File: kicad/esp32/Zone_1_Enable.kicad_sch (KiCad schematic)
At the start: 5 parts, among them SW201 B3F-1150

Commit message: Created rev 1.01 - Addes some more labels and annotations
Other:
- title: (none) -> TL2C-ESP32-1 TL2C Adapter for ESP32
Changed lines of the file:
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@@
 	(generator "eeschema")
 	(generator_version "8.0")
-	(paper "A4")
+	(paper "A3")
+	(title_block
+		(title "TL2C-ESP32-1 TL2C Adapter for ESP32")
+		(date "2024-02-08")
+		(rev "1.01")
+	)
 	(junction
 		(at 107.95 62.23)

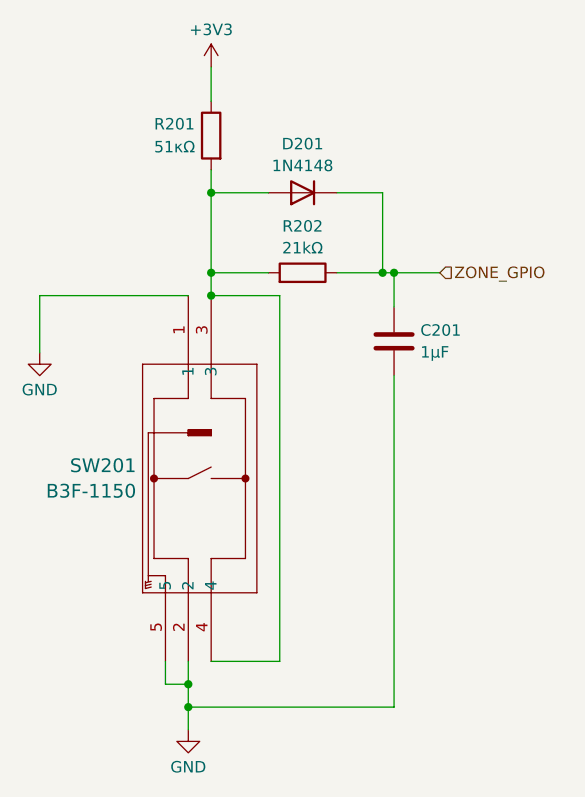
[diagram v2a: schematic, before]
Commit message: Reseated the RJ45
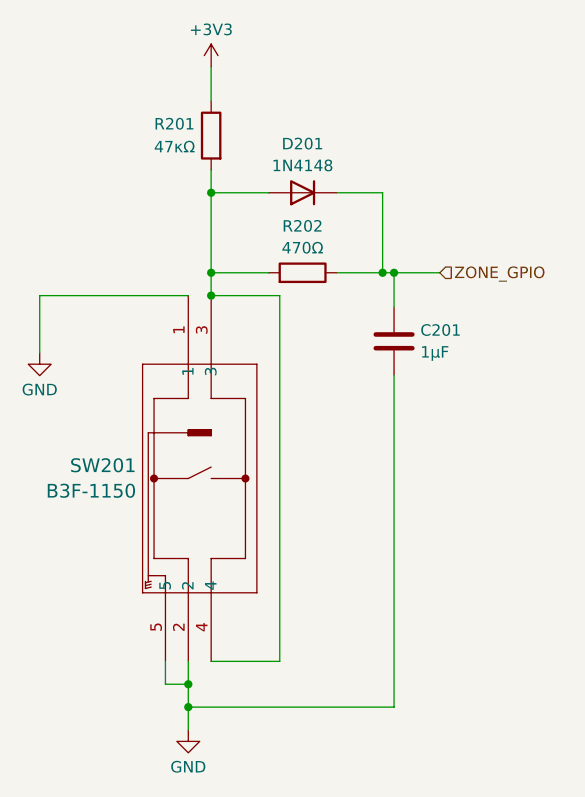
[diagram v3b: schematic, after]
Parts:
- R201: value 51κΩ -> 47κΩ
- R202: value 21kΩ -> 470Ω

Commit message: R1 correction
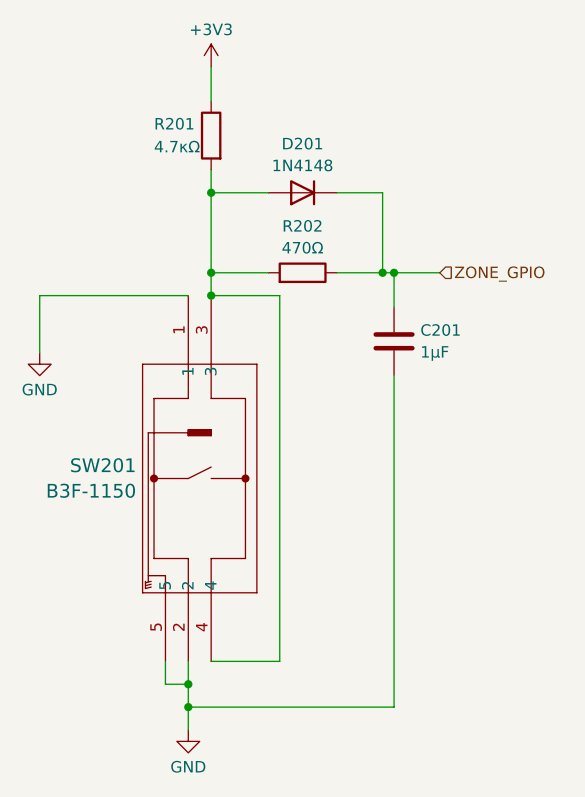
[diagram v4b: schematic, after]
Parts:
- R201: value 47κΩ -> 4.7κΩ
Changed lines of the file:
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@@
 			)
 		)
-		(property "Value" "47κΩ"
+		(property "Value" "4.7κΩ"
 			(at 82.55 48.26 0)
 			(effects

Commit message: Adding some documentation
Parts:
- C201: value 1μF -> 0.1μF
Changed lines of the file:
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@@
 		(fields_autoplaced yes)
 		(property "Reference" "C201"
-			(at 112.141 68.6379 0)
+			(at 112.141 68.6378 0)
 			(effects
 				(font
@@
 			)
 		)
-		(property "Value" "1μF"
+		(property "Value" "0.1μF"
 			(at 112.141 71.0621 0)
 			(effects

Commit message: Updated the artwork and documentation
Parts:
- R201: value 4.7κΩ -> 10κΩ
- R202: value 470Ω -> 10κΩ
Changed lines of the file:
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@@
 			)
 		)
-		(property "Value" "4.7κΩ"
+		(property "Value" "10κΩ"
 			(at 82.55 48.26 0)
 			(effects
@@
 			)
 		)
-		(property "Value" "470Ω"
+		(property "Value" "10κΩ"
 			(at 99.06 59.4938 90)
 			(effects
